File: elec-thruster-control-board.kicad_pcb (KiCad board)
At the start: 2 copper layers, 55.5 x 67 mm, 59 parts, among them J1 gp15-pwm7B, J11 gp17-pwm0B, J12 gp2-pwm1A, J13 Conn_01x07, J15 gp6-pwm3A, J16 gp8-pwm4A, J18 gp19-pwm1B, J19 gp21-pwm2B, J2 gp0-pwm0A, J20 gp26-pwm5A, J21 gp27-pwm5B, J22 Conn_01x06, J24 Conn_01x06, J3 gp10-pwm5A, J4 Conn_01x20_Socket, J5 gp4-pwm2A, J6 Conn_01x20_Socket

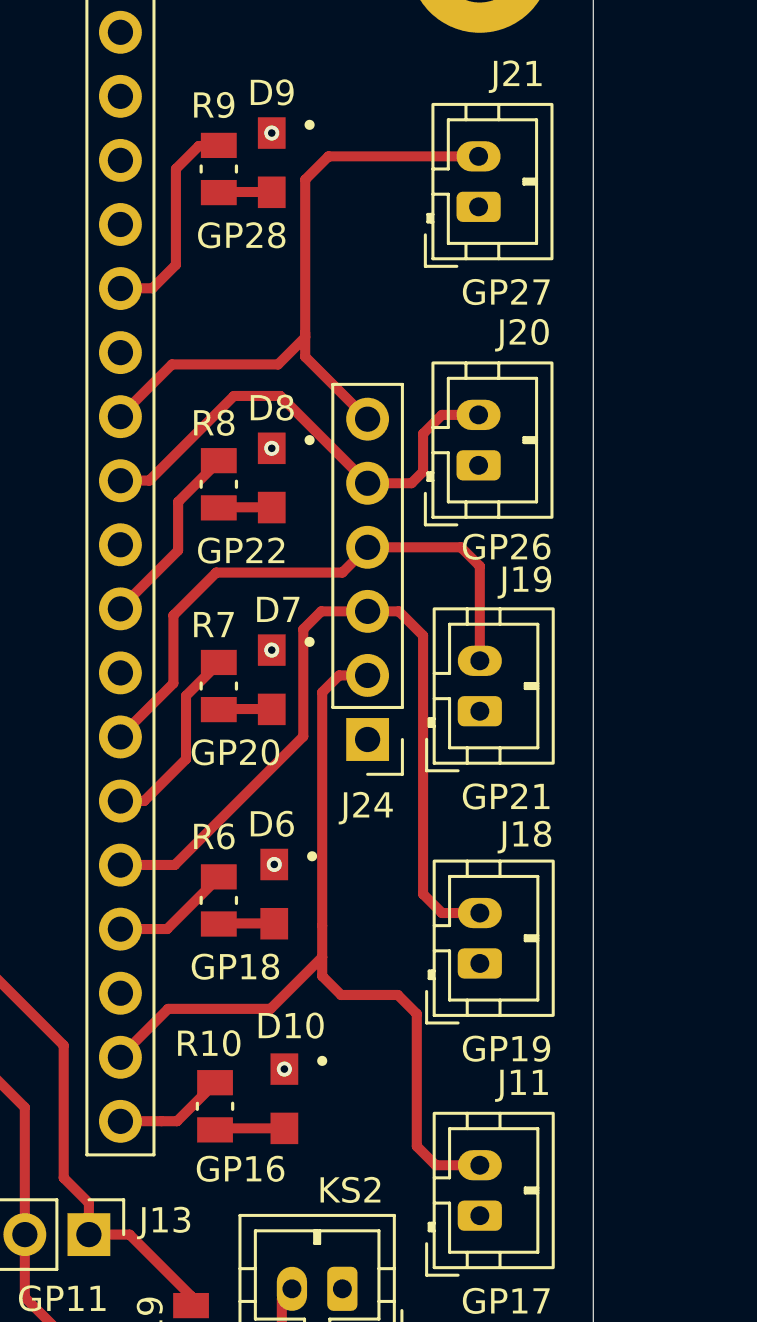
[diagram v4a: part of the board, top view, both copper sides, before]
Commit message: Cleaned up trace spacing
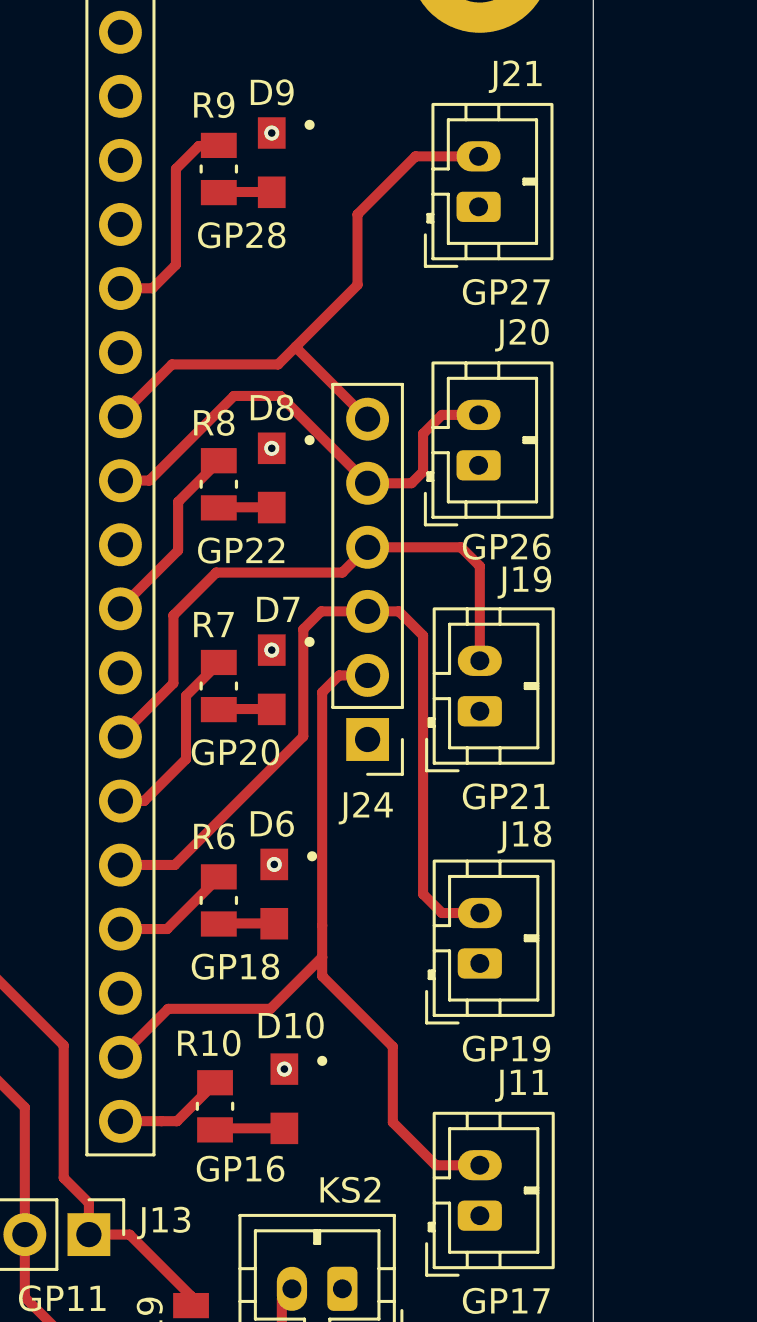
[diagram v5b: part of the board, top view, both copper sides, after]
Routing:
- net /gp27-pwm5B: track 26.6 -> 24.2 mm
- net /gp17-pwm0B: track 35.4 -> 34.1 mm
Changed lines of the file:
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@@
 	)
 	(segment
-		(start 160.25 100.25)
+		(start 159.3 99.3)
 		(end 161 101)
+		(width 0.4)
+		(layer "F.Cu")
+		(net 1)
+	)
+	(segment
+		(start 156.5 93.5)
+		(end 159.3 96.3)
 		(width 0.4)
 		(layer "F.Cu")
@@
 	)
 	(segment
-		(start 157.25 94.25)
-		(end 159.5 94.25)
-		(width 0.4)
-		(layer "F.Cu")
-		(net 1)
-	)
-	(segment
 		(start 156.5 91.5)
 		(end 156.5 82.25)
@@
 	)
 	(segment
-		(start 159.5 94.25)
-		(end 160.25 95)
-		(width 0.4)
-		(layer "F.Cu")
-		(net 1)
-	)
-	(segment
 		(start 156.5 82.25)
 		(end 157.17 81.58)
@@
 	)
 	(segment
-		(start 160.25 95)
-		(end 160.25 100.25)
+		(start 159.3 96.3)
+		(end 159.3 99.3)
 		(width 0.4)
 		(layer "F.Cu")
@@
 	)
 	(segment
-		(start 156.5 93.5)
-		(end 157.25 94.25)
-		(width 0.4)
-		(layer "F.Cu")
-		(net 1)
-	)
-	(segment
 		(start 120.8 76.16)
 		(end 118.84 76.16)
@@
 	)
 	(segment
-		(start 155.82625 68)
-		(end 155.82625 68.94625)
+		(start 148.5 71.31)
+		(end 148.5 71.2925)
+		(width 0.4)
+		(layer "F.Cu")
+		(net 10)
+	)
+	(segment
+		(start 160.2 61)
+		(end 157.9 63.3)
 		(width 0.4)
 		(layer "F.Cu")
@@
 	)
 	(segment
-		(start 155.82625 68.94625)
-		(end 158.3 71.42)
-		(width 0.4)
-		(layer "F.Cu")
-		(net 10)
-	)
-	(segment
-		(start 155.82625 61.92375)
-		(end 156.75 61)
-		(width 0.4)
-		(layer "F.Cu")
-		(net 10)
-	)
-	(segment
-		(start 156.75 61)
-		(end 162.7 61)
+		(start 162.7 61)
+		(end 160.2 61)
+		(width 0.4)
+		(layer "F.Cu")
+		(net 10)
+	)
+	(segment
+		(start 157.9 66.1)
+		(end 155.45 68.55)
+		(width 0.4)
+		(layer "F.Cu")
+		(net 10)
+	)
+	(segment
+		(start 155.45 68.57)
+		(end 155.45 68.55)
+		(width 0.4)
+		(layer "F.Cu")
+		(net 10)
+	)
+	(segment
+		(start 157.9 63.3)
+		(end 157.9 66.1)
 		(width 0.4)
 		(layer "F.Cu")
@@
 	(segment
 		(start 154.75 69.25)
-		(end 155.82625 68.17375)
-		(width 0.4)
-		(layer "F.Cu")
-		(net 10)
-	)
-	(segment
-		(start 148.5 71.31)
-		(end 148.5 71.2925)
+		(end 155.45 68.55)
+		(width 0.4)
+		(layer "F.Cu")
+		(net 10)
+	)
+	(segment
+		(start 158.3 71.42)
+		(end 155.45 68.57)
 		(width 0.4)
 		(layer "F.Cu")
@@
 		(width 0.4)
 		(layer "F.Cu")
-		(net 10)
-	)
-	(segment
-		(start 155.82625 68.17375)
-		(end 155.82625 61.92375)
-		(width 0.4)
-		(layer "F.Cu")

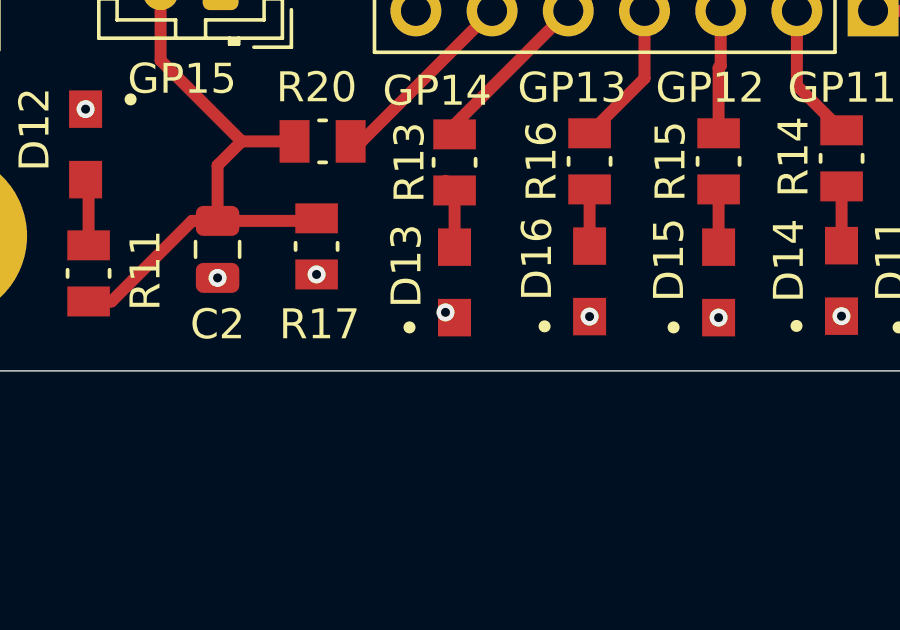
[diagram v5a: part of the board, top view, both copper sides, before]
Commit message: Added Assembly Notes to board (Listed under the user comments layer)
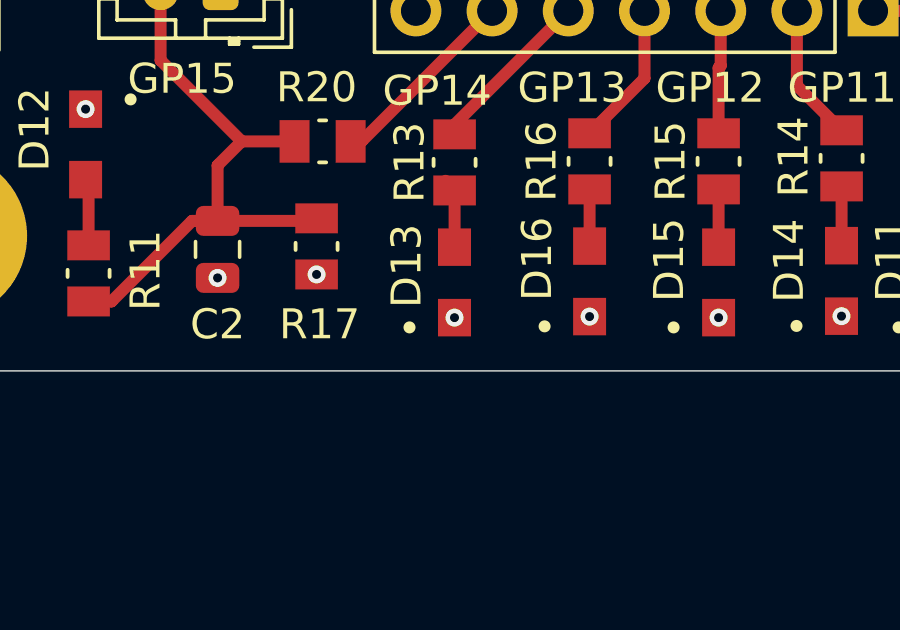
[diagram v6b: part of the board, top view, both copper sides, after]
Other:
- board text added: "Assembly Notes: Dot next to LED pad signifies negative terminal/Lower potential"
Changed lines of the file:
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@@
+		)
+	)
+	(gr_text "Assembly Notes:\nDot next to LED pad signifies negative terminal/Lower potential"
+		(at 184.3 51.5 0)
+		(layer "Cmts.User")
+		(effects
+			(font
+				(size 1 1)
+				(thickness 0.15)
+			)
+			(justify left bottom)
 		)
 	)
@@
 	)
 	(via
-		(at 132.9969 113.79875)
-		(size 0.6)
-		(drill 0.3)
+		(at 133.2969 113.975)
+		(size 0.6)
+		(drill 0.3)
